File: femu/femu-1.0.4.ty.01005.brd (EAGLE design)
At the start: 24.1 x 15.8 mm, 56 parts, among them IC1 ESP32-QFN_5X5

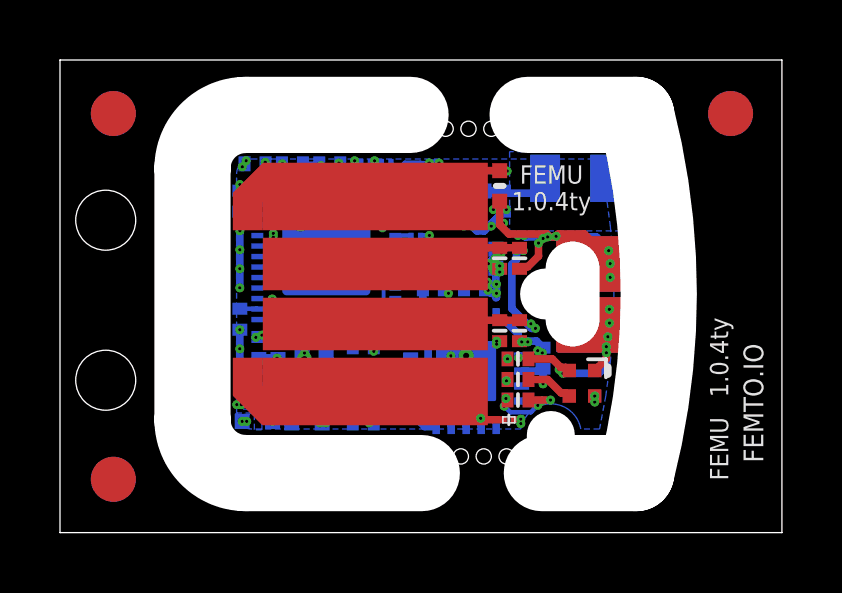
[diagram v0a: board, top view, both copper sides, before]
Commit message: Adjusting antenna and ground plane in femu-1.0.4.ty.01005 design. 11.35mil wide RF trace, 5mil isolation. At PCBWay 0.8mm thick PCB (0.175mm thick dialectric, constant 4.29)(copper thickness of 18um) ...should yield 50ohm impedance at 2448MHz (2.4GHz)
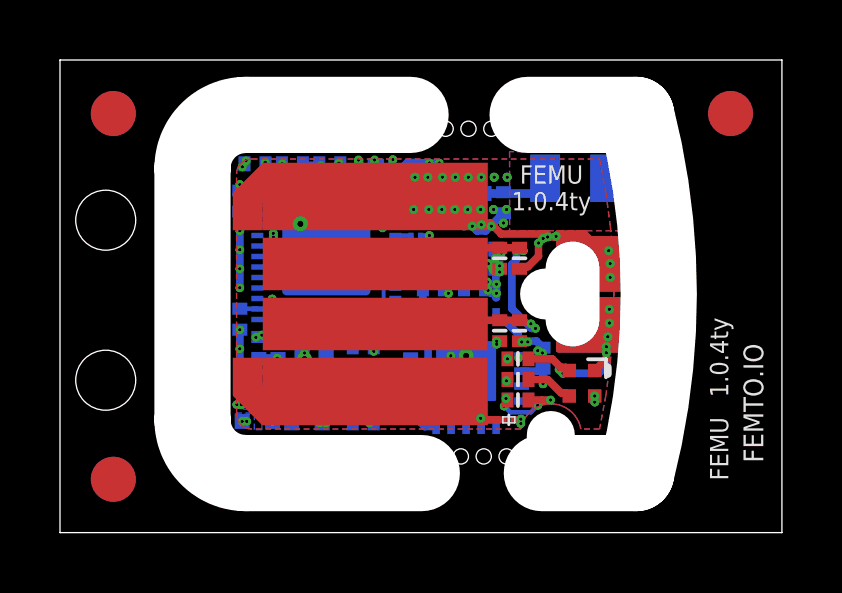
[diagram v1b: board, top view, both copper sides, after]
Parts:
- removed FB2: (no value), microbuilder:_0402MP
- moved C13 0.29 mm to (11.8, 12.2)
- moved C8 0.08 mm to (13.8, 11.3)
- moved C9 0.05 mm to (14.8, 11.0)
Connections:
- removed net N$11: FB2.1, U$37.1/GND
- net GND: now also U$37.1/GND; no longer FB2.2
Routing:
- net N$11: track 4.50 -> 0.00 mm
- net GND: track 94.2 -> 97.7 mm, vias 124 -> 145
- net IO26/DAC2: track 12.6 -> 11.5 mm, vias 9 -> 7
- net 3.3V: track 56.0 -> 56.6 mm
- net ANT: track 2.95 -> 2.35 mm
- net N$6: track 2.86 -> 2.29 mm
- net IO27/R: track 19.7 -> 19.4 mm, vias 16 -> 17
- added copper zone on layer 1, net GND

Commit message: Adjusting ground pours.
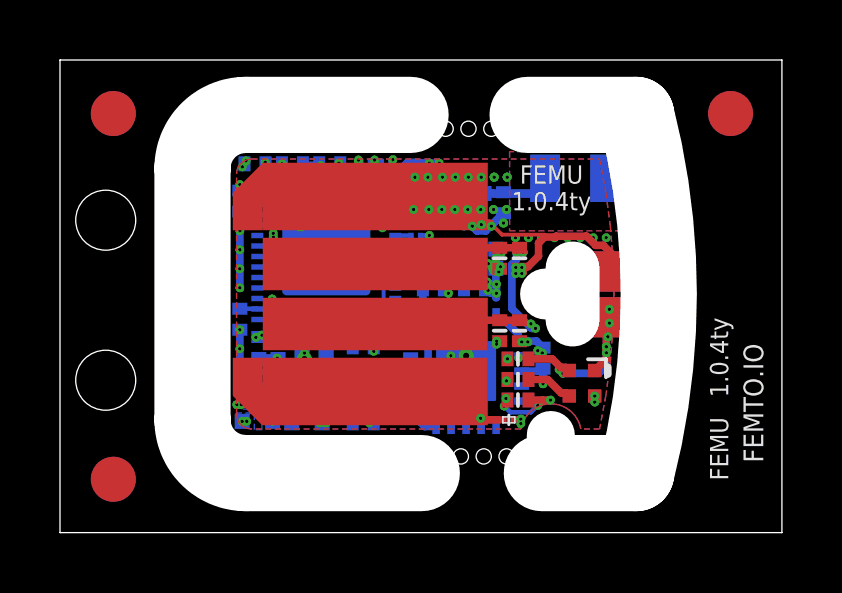
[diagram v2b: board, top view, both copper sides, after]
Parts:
- U$6: value FEMU-EDGE-CONNECTOR -> FEMU-EDGE-CONNECTORFEMU-EDGE-CONN-SLIM; device femu-edge-connectors:FEMU-EDGE-CONNECTOR -> femu-edge-connectors:FEMU-EDGE-CONN-SLIM
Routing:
- net GND: track 97.7 -> 95.4 mm, vias 145 -> 150
- net IO26/DAC2: vias 7 -> 11

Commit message: Adjusted trace width and distance for 35ohm impedance
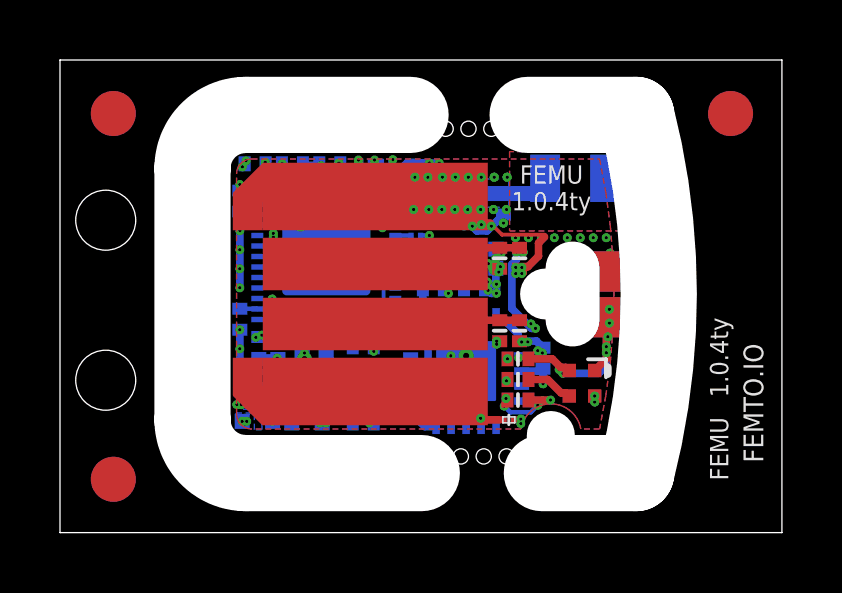
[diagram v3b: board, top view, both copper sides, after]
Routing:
- net GND: track 95.4 -> 90.1 mm
